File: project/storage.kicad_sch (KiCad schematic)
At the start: 29 parts

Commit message: configuring kibot for both projects
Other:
- title: space -> storage
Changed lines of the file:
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@@
   (paper "A4")
   (title_block
-    (title "space")
-    (date "2024-02-05")
+    (title "storage")
+    (date "2024-02-16")
     (rev "5.0")
     (company "makerspace.lt")

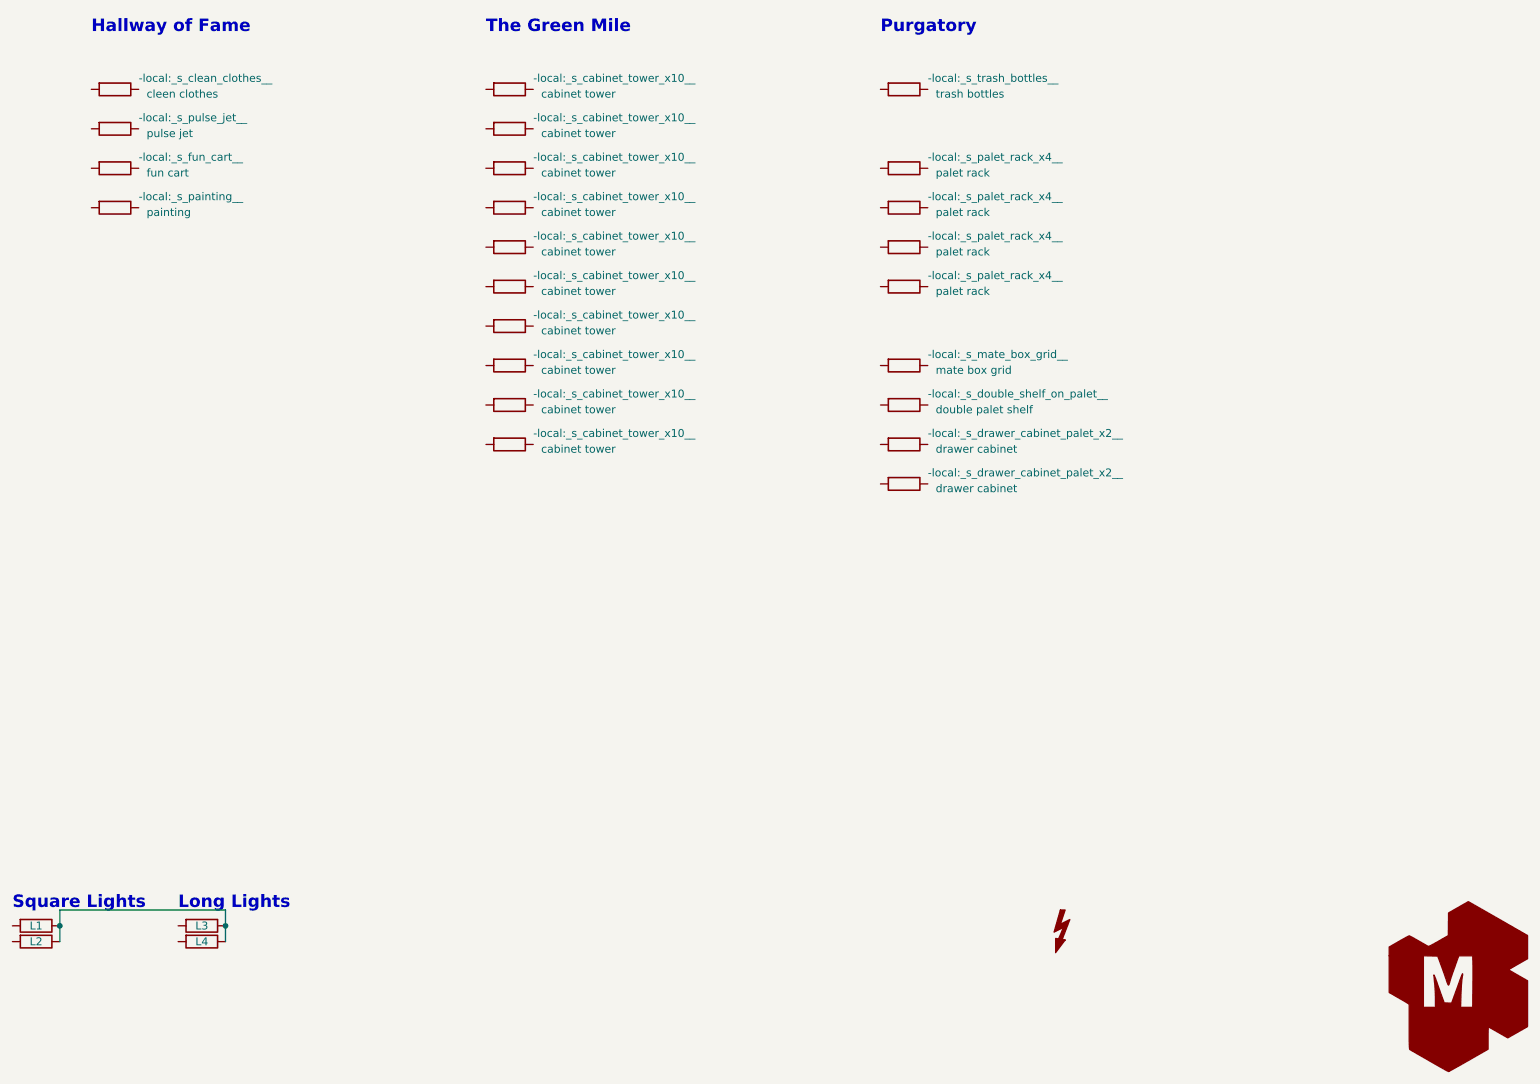
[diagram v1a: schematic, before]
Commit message: fixing electric channel dimensions
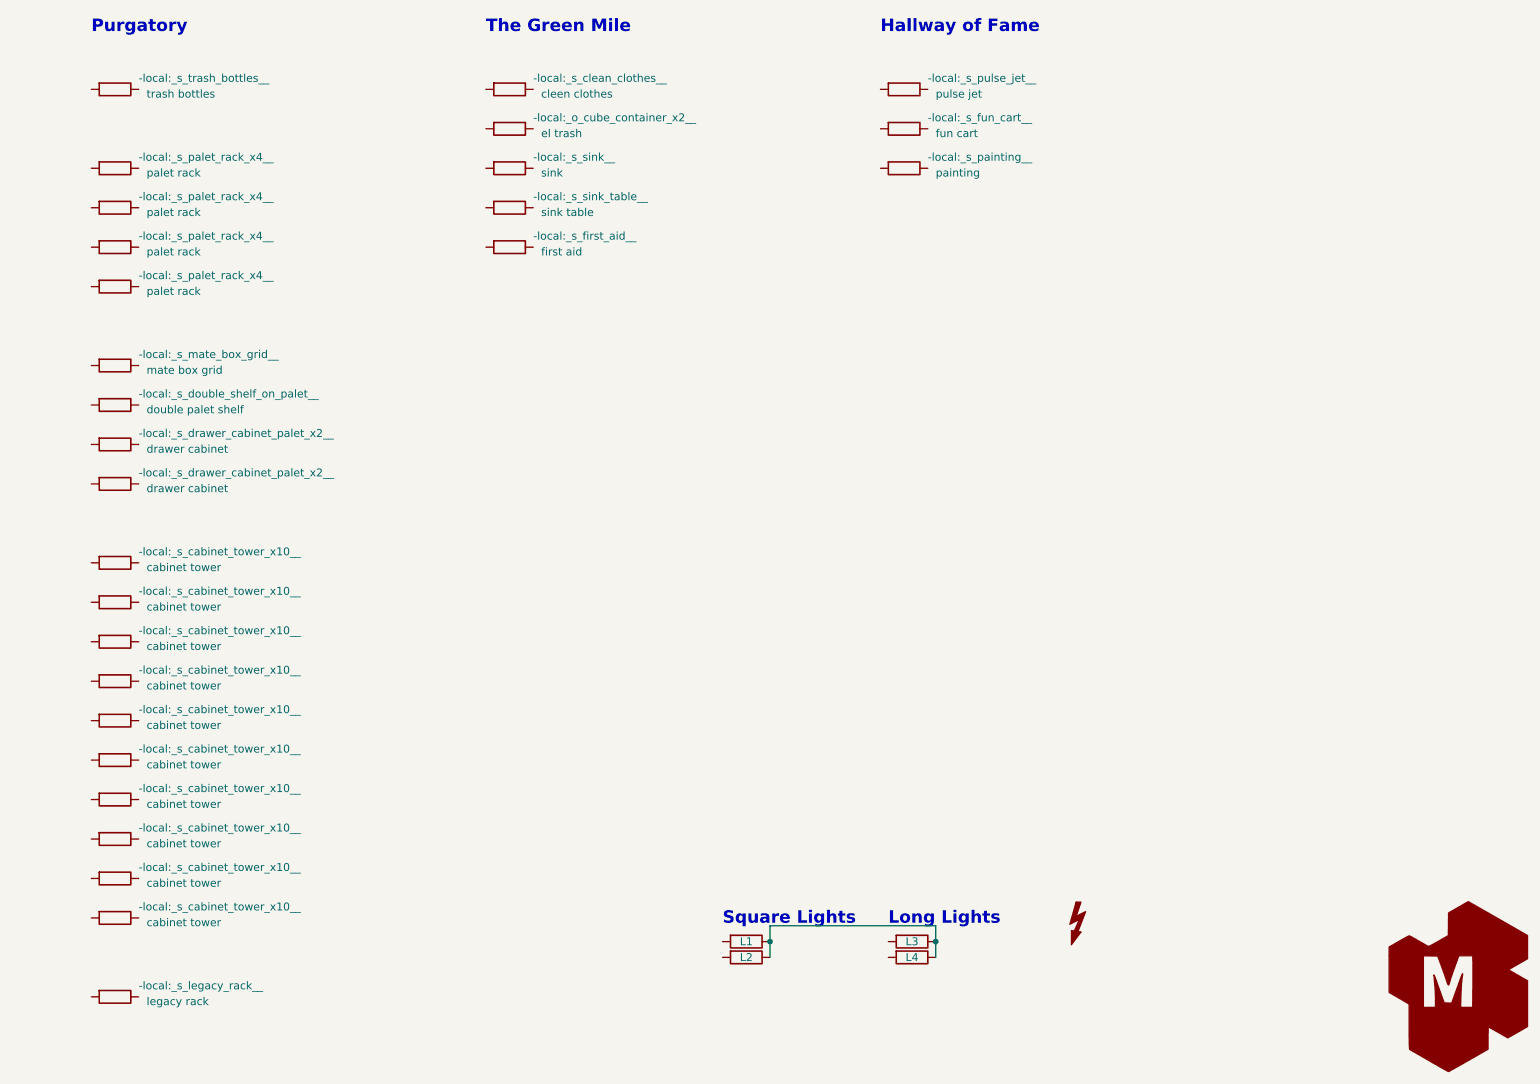
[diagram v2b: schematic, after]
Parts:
- added R20: legacy rack, -local:_s_legacy_rack__, symbol Device:R
- added R22: el trash, -local:_o_cube_container_x2__, symbol Device:R
- added R23: sink, -local:_s_sink__, symbol Device:R
- added R24: sink table, -local:_s_sink_table__, symbol Device:R
- added R25: first aid, -local:_s_first_aid__, symbol Device:R
- renumbered R15 to R1, R5 to R10, R6 to R11, R7 to R12, R8 to R13, R9 to R14, R10 to R15, R11 to R16, R12 to R17, R13 to R18, R14 to R19, R16 to R2, R1 to R21, R2 to R26, R3 to R27, R4 to R28, R17 to R3, R18 to R4, R19 to R5, R20 to R6, R21 to R7, R22 to R8, R23 to R9
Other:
- moved on the sheet: L1, L2, L3, L4
